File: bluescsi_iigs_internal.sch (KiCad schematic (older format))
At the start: 16 parts, among them J1 Conn_02x13_Top_Bottom, J2 Conn_02x13_Top_Bottom, J3 Micro_SD_Card, SW1 SW_SPDT, U1 YAAJ_BluePill, U2 UCC5606, U3 UCC5606

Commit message: V1.1 from v1.0 Fix IDC26 pin header to be correct! Change capacitor footprint to handsolder variant. Move mounting holes toward centre by about 2.54 and back by 2.54
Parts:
- C1, C2, C3: footprint Capacitor_Tantalum_SMD:CP_EIA-3528-21_Kemet-B -> Capacitor_Tantalum_SMD:CP_EIA-3528-21_Kemet-B_Pad1.50x2.35mm_HandSolder
- J1, J2: value Conn_02x13_Top_Bottom -> Conn_02x13_Odd_Even; symbol Connector_Generic:Conn_02x13_Top_Bottom -> Connector_Generic:Conn_02x13_Odd_Even
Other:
- moved on the sheet: D2, H1, H2, J3, R2, SW1

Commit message: Change switch to smd
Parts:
- SW1: footprint Connector_PinHeader_2.54mm:PinHeader_1x03_P2.54mm_Horizontal -> Button_Switch_SMD:SW_SPDT_PCM12
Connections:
- net +5V: now also SW1.3 (C); no longer SW1.1 (A)
- net GND: now also SW1.1 (A); no longer SW1.3 (C)
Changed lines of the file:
@@
 $EndComp
 $Comp
-L Switch:SW_SPDT SW1
-U 1 1 6062FC1A
-P 7300 1300
-F 0 "SW1" H 7300 1585 50  0000 C CNN
-F 1 "SW_SPDT" H 7300 1494 50  0000 C CNN
-F 2 "Connector_PinHeader_2.54mm:PinHeader_1x03_P2.54mm_Horizontal" H 7300 1300 50  0001 C CNN
-F 3 "~" H 7300 1300 50  0001 C CNN
-	1    7300 1300
-	1    0    0    -1
-$EndComp
-$Comp
 L Device:LED D2
 U 1 1 60631033
@@
 Text Label 1100 2050 2    50   ~ 0
 SCSI_DB6
+$Comp
+L Switch:SW_SPDT SW1
+U 1 1 6062FC1A
+P 7300 1300
+F 0 "SW1" H 7300 1585 50  0000 C CNN
+F 1 "SW_SPDT" H 7300 1494 50  0000 C CNN
+F 2 "Button_Switch_SMD:SW_SPDT_PCM12" H 7300 1300 50  0001 C CNN
+F 3 "~" H 7300 1300 50  0001 C CNN
+	1    7300 1300
+	1    0    0    1
+$EndComp
 $EndSCHEMATC

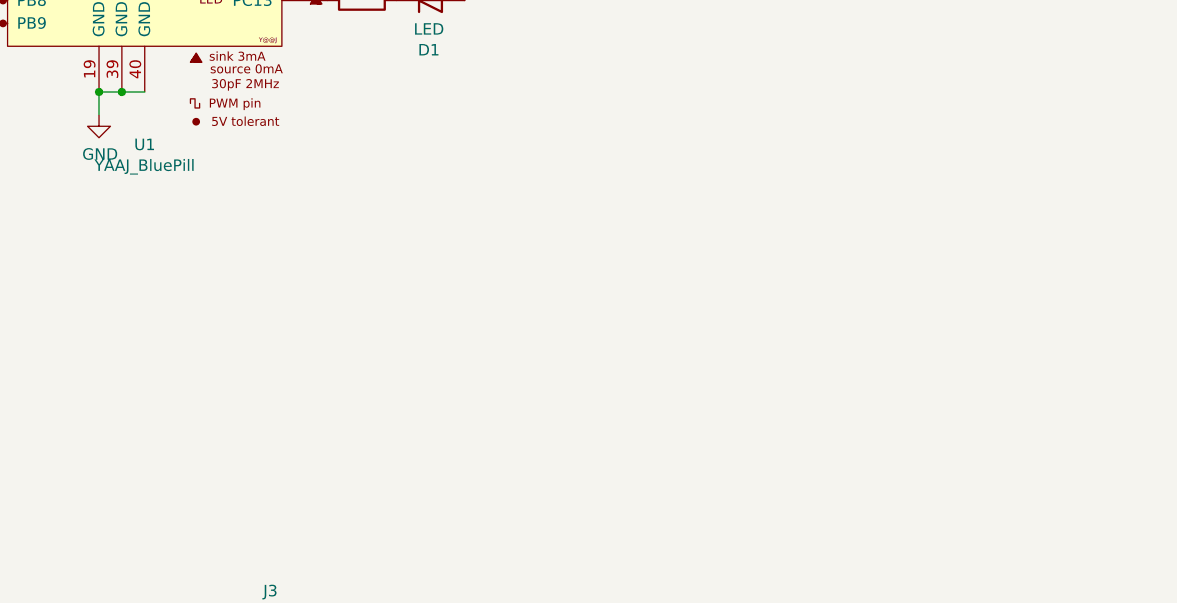
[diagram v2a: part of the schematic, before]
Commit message: Add auxilliary 12v input
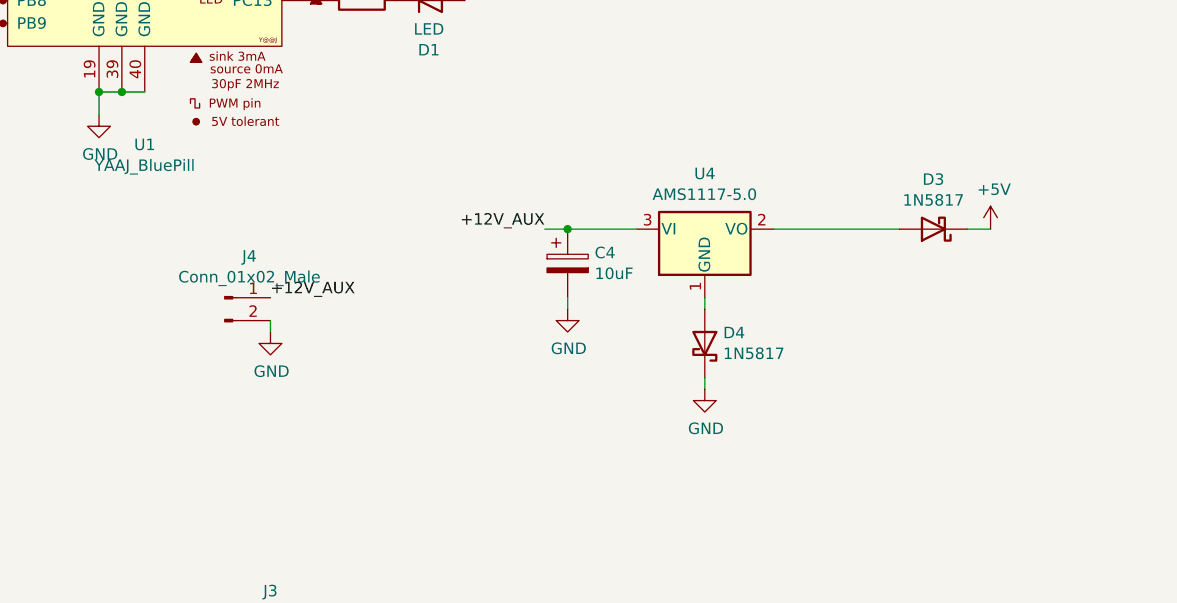
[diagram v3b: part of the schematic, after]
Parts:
- added C4: 10uF, Capacitor_Tantalum_SMD:CP_EIA-3528-21_Kemet-B_Pad1.50x2.35mm_HandSolder, symbol Device:CP
- added D3, D4: 1N5817, Diode_SMD:D_MicroMELF, symbol Device:D_Schottky
- added J4: Conn_01x02_Male, Connector_PinHeader_2.54mm:PinHeader_1x02_P2.54mm_Vertical, symbol Connector:Conn_01x02_Male
- added U4: AMS1117-5.0, Package_TO_SOT_SMD:SOT-223-3_TabPin2, symbol Regulator_Linear:AMS1117-5.0
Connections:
- net +5V: now also D3.1 (K)
- net GND: now also C4.2, D4.1 (K), J4.2 (Pin_2)
- new net: D4.2 (A), U4.1 (GND)
- new net: D3.2 (A), U4.2 (VO)
- new net +12V_AUX: C4.1, J4.1 (Pin_1), U4.3 (VI)
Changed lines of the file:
@@
 	1    0    0    1
 $EndComp
+$Comp
+L Regulator_Linear:AMS1117-5.0 U4
+U 1 1 608623C0
+P 7750 4550
+F 0 "U4" H 7750 4792 50  0000 C CNN
+F 1 "AMS1117-5.0" H 7750 4701 50  0000 C CNN
+F 2 "Package_TO_SOT_SMD:SOT-223-3_TabPin2" H 7750 4750 50  0001 C CNN
+F 3 "http://www.advanced-monolithic.com/pdf/ds1117.pdf" H 7850 4300 50  0001 C CNN
+	1    7750 4550
+	1    0    0    -1
+$EndComp
+$Comp
+L Device:CP C4
+U 1 1 608634DB
+P 7150 4700
+F 0 "C4" H 7268 4746 50  0000 L CNN
+F 1 "10uF" H 7268 4655 50  0000 L CNN
+F 2 "Capacitor_Tantalum_SMD:CP_EIA-3528-21_Kemet-B_Pad1.50x2.35mm_HandSolder" H 7188 4550 50  0001 C CNN
+F 3 "~" H 7150 4700 50  0001 C CNN
+	1    7150 4700
+	1    0    0    -1
+$EndComp
+$Comp
+L Connector:Conn_01x02_Male J4
+U 1 1 60864BE9
+P 5650 4850
+F 0 "J4" H 5758 5031 50  0000 C CNN
+F 1 "Conn_01x02_Male" H 5758 4940 50  0000 C CNN
+F 2 "Connector_PinHeader_2.54mm:PinHeader_1x02_P2.54mm_Vertical" H 5650 4850 50  0001 C CNN
+F 3 "~" H 5650 4850 50  0001 C CNN
+	1    5650 4850
+	1    0    0    -1
+$EndComp
+$Comp
+L power:GND #PWR0119
+U 1 1 60865DDA
+P 5850 5000
+F 0 "#PWR0119" H 5850 4750 50  0001 C CNN
+F 1 "GND" H 5855 4827 50  0000 C CNN
+F 2 "" H 5850 5000 50  0001 C CNN
+F 3 "" H 5850 5000 50  0001 C CNN
+	1    5850 5000
+	1    0    0    -1
+$EndComp
+$Comp
+L power:GND #PWR0120
+U 1 1 6086659F
+P 7150 4900
+F 0 "#PWR0120" H 7150 4650 50  0001 C CNN
+F 1 "GND" H 7155 4727 50  0000 C CNN
+F 2 "" H 7150 4900 50  0001 C CNN
+F 3 "" H 7150 4900 50  0001 C CNN
+	1    7150 4900
+	1    0    0    -1
+$EndComp
+$Comp
+L power:GND #PWR0121
+U 1 1 60866B00
+P 7750 5250
+F 0 "#PWR0121" H 7750 5000 50  0001 C CNN
+F 1 "GND" H 7755 5077 50  0000 C CNN
+F 2 "" H 7750 5250 50  0001 C CNN
+F 3 "" H 7750 5250 50  0001 C CNN
+	1    7750 5250
+	1    0    0    -1
+$EndComp
+Wire Wire Line
+	5850 4950 5850 5000
+Text Label 5850 4850 0    50   ~ 0
++12V_AUX
+Text Label 7050 4550 2    50   ~ 0
++12V_AUX
+Wire Wire Line
+	7050 4550 7150 4550
+Wire Wire Line
+	7150 4550 7450 4550
+Connection ~ 7150 4550
+Wire Wire Line
+	7150 4850 7150 4900
+Wire Wire Line
+	7750 4850 7750 4900
+$Comp
+L Device:D_Schottky D3
+U 1 1 6086E55B
+P 8750 4550
+F 0 "D3" H 8750 4333 50  0000 C CNN
+F 1 "1N5817" H 8750 4424 50  0000 C CNN
+F 2 "Diode_SMD:D_MicroMELF" H 8750 4550 50  0001 C CNN
+F 3 "~" H 8750 4550 50  0001 C CNN
+	1    8750 4550
+	-1   0    0    1
+$EndComp
+$Comp
+L Device:D_Schottky D4
+U 1 1 6086EF1B
+P 7750 5050
+F 0 "D4" V 7796 5130 50  0000 L CNN
+F 1 "1N5817" V 7705 5130 50  0000 L CNN
+F 2 "Diode_SMD:D_MicroMELF" H 7750 5050 50  0001 C CNN
+F 3 "~" H 7750 5050 50  0001 C CNN
+	1    7750 5050
+	0    1    -1   0
+$EndComp
+Wire Wire Line
+	7750 5200 7750 5250
+$Comp
+L power:+5V #PWR0123
+U 1 1 6087347C
+P 9000 4550
+F 0 "#PWR0123" H 9000 4400 50  0001 C CNN
+F 1 "+5V" H 9015 4723 50  0000 C CNN
+F 2 "" H 9000 4550 50  0001 C CNN
+F 3 "" H 9000 4550 50  0001 C CNN
+	1    9000 4550
+	1    0    0    -1
+$EndComp
+Wire Wire Line
+	8900 4550 9000 4550
+Wire Wire Line
+	8050 4550 8600 4550
 $EndSCHEMATC

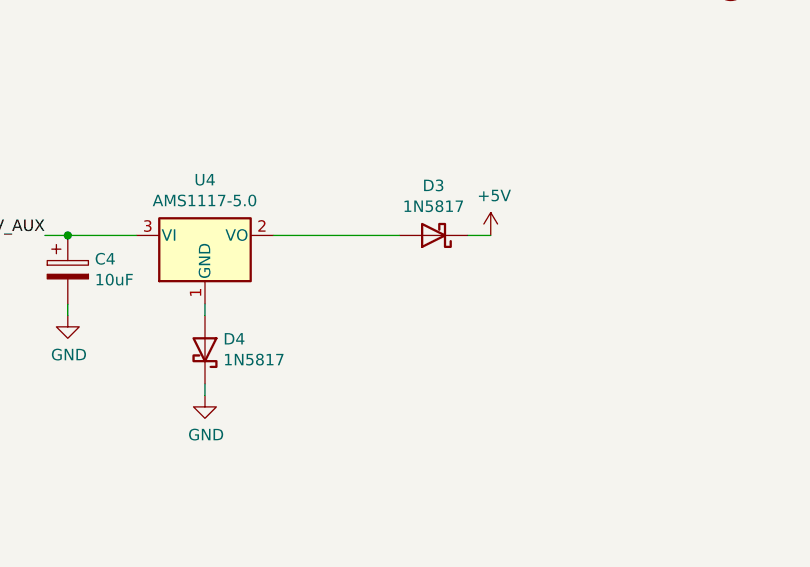
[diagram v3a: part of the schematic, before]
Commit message: Change footprint of diodes
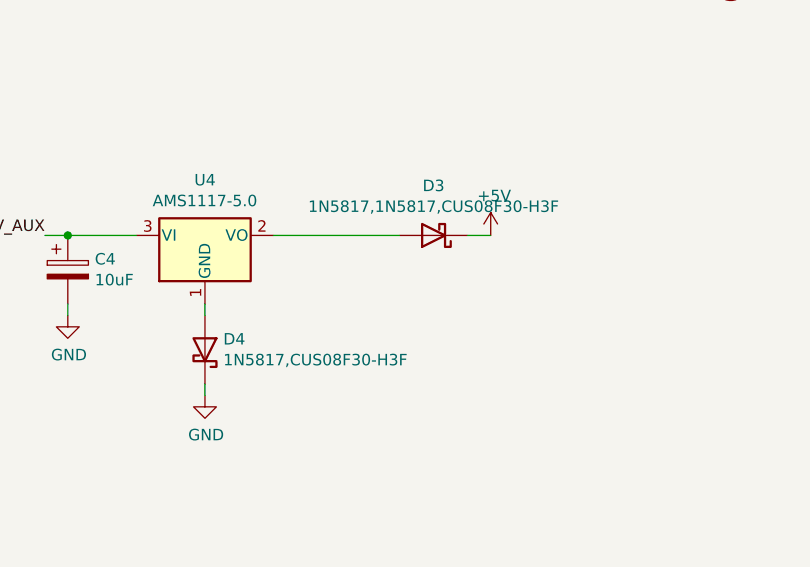
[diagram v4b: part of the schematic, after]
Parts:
- D3: value 1N5817 -> 1N5817,1N5817,CUS08F30-H3F; footprint Diode_SMD:D_MicroMELF -> Diode_SMD:D_SOD-323_HandSoldering
- D4: value 1N5817 -> 1N5817,CUS08F30-H3F; footprint Diode_SMD:D_MicroMELF -> Diode_SMD:D_SOD-323_HandSoldering
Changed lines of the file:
@@
 P 8750 4550
 F 0 "D3" H 8750 4333 50  0000 C CNN
-F 1 "1N5817" H 8750 4424 50  0000 C CNN
-F 2 "Diode_SMD:D_MicroMELF" H 8750 4550 50  0001 C CNN
+F 1 "1N5817,1N5817,CUS08F30-H3F" H 8750 4424 50  0000 C CNN
+F 2 "Diode_SMD:D_SOD-323_HandSoldering" H 8750 4550 50  0001 C CNN
 F 3 "~" H 8750 4550 50  0001 C CNN
 	1    8750 4550
@@
 P 7750 5050
 F 0 "D4" V 7796 5130 50  0000 L CNN
-F 1 "1N5817" V 7705 5130 50  0000 L CNN
-F 2 "Diode_SMD:D_MicroMELF" H 7750 5050 50  0001 C CNN
+F 1 "1N5817,CUS08F30-H3F" V 7705 5130 50  0000 L CNN
+F 2 "Diode_SMD:D_SOD-323_HandSoldering" H 7750 5050 50  0001 C CNN
 F 3 "~" H 7750 5050 50  0001 C CNN
 	1    7750 5050

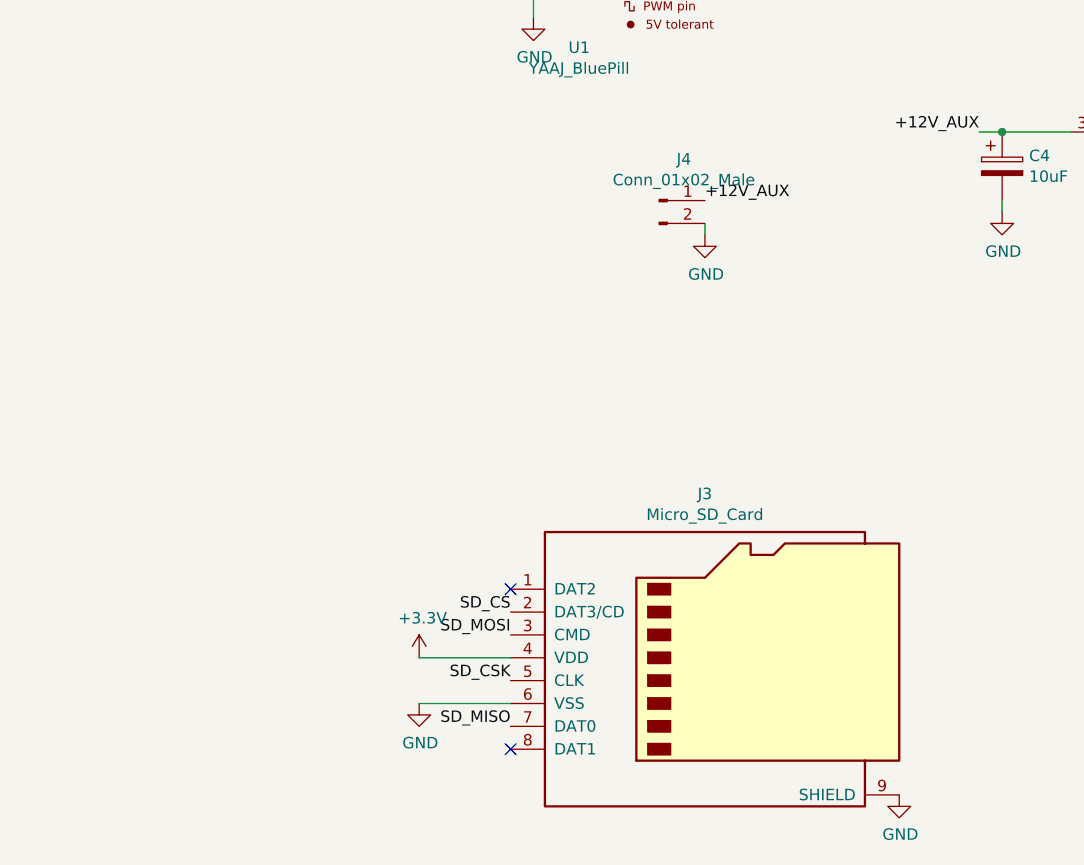
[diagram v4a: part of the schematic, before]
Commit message: Change microsd slot to Molex 105162-0001. Add version number to back silkscreen
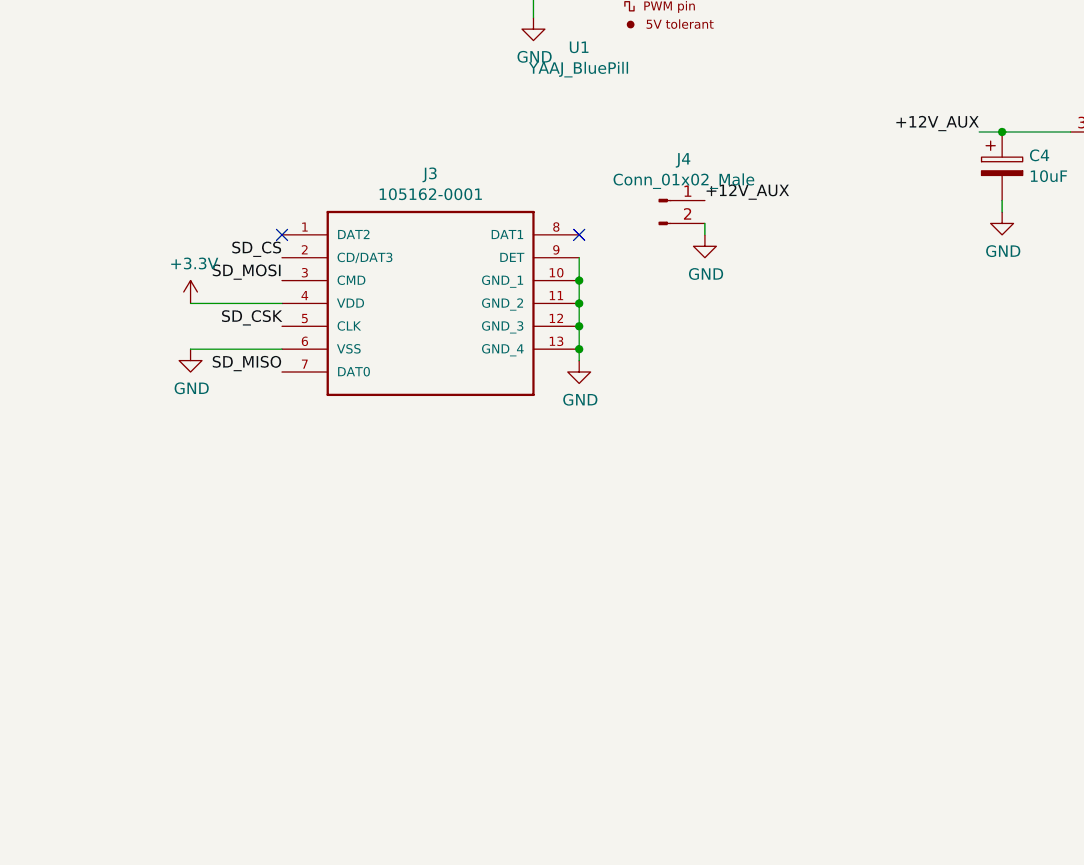
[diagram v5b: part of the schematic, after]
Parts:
- removed J3: Micro_SD_Card, Connector_Card:microSD_HC_Molex_104031-0811, symbol Connector:Micro_SD_Card
- added J3: 105162-0001, 105162-0001, symbol 105162-0001:105162-0001
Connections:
- net +3V3: now also J3.4 (VDD)
- net GND: now also J3.10 (GND_1), J3.11 (GND_2), J3.12 (GND_3), J3.13 (GND_4), J3.6 (VSS), J3.9 (DET)
- net SD_CS: now also J3.2 (CD/DAT3)
- net SD_CSK: now also J3.5 (CLK)
- net SD_MISO: now also J3.7 (DAT0)
- net SD_MOSI: now also J3.3 (CMD)
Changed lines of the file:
@@
 L power:+3.3V #PWR0105
 U 1 1 6061CFE5
-P 4600 6850
-F 0 "#PWR0105" H 4600 6700 50  0001 C CNN
-F 1 "+3.3V" H 4615 7023 50  0000 C CNN
-F 2 "" H 4600 6850 50  0001 C CNN
-F 3 "" H 4600 6850 50  0001 C CNN
-	1    4600 6850
+P 3600 5300
+F 0 "#PWR0105" H 3600 5150 50  0001 C CNN
+F 1 "+3.3V" H 3615 5473 50  0000 C CNN
+F 2 "" H 3600 5300 50  0001 C CNN
+F 3 "" H 3600 5300 50  0001 C CNN
+	1    3600 5300
 	1    0    0    -1
 $EndComp
@@
 SD_MOSI
 $Comp
-L Connector:Micro_SD_Card J3
-U 1 1 6062225F
-P 5900 6850
-F 0 "J3" H 5850 7567 50  0000 C CNN
-F 1 "Micro_SD_Card" H 5850 7476 50  0000 C CNN
-F 2 "Connector_Card:microSD_HC_Molex_104031-0811" H 7050 7150 50  0001 C CNN
-F 3 "http://katalog.we-online.de/em/datasheet/693072010801.pdf" H 5900 6850 50  0001 C CNN
-	1    5900 6850
-	1    0    0    -1
-$EndComp
-$Comp
 L power:GND #PWR0108
 U 1 1 60623212
-P 4600 7050
-F 0 "#PWR0108" H 4600 6800 50  0001 C CNN
-F 1 "GND" H 4605 6877 50  0000 C CNN
-F 2 "" H 4600 7050 50  0001 C CNN
-F 3 "" H 4600 7050 50  0001 C CNN
-	1    4600 7050
+P 5300 5550
+F 0 "#PWR0108" H 5300 5300 50  0001 C CNN
+F 1 "GND" H 5305 5377 50  0000 C CNN
+F 2 "" H 5300 5550 50  0001 C CNN
+F 3 "" H 5300 5550 50  0001 C CNN
+	1    5300 5550
 	1    0    0    -1
 $EndComp
-Text Label 5000 6650 2    50   ~ 0
+Text Label 4000 5100 2    50   ~ 0
 SD_CS
-Text Label 5000 6950 2    50   ~ 0
+Text Label 4000 5400 2    50   ~ 0
 SD_CSK
-Text Label 5000 7150 2    50   ~ 0
+Text Label 4000 5600 2    50   ~ 0
 SD_MISO
-Text Label 5000 6750 2    50   ~ 0
+Text Label 4000 5200 2    50   ~ 0
 SD_MOSI
-$Comp
-L power:GND #PWR0109
-U 1 1 60623E38
-P 6700 7450
-F 0 "#PWR0109" H 6700 7200 50  0001 C CNN
-F 1 "GND" H 6705 7277 50  0000 C CNN
-F 2 "" H 6700 7450 50  0001 C CNN
-F 3 "" H 6700 7450 50  0001 C CNN
-	1    6700 7450
-	1    0    0    -1
-$EndComp
-Wire Wire Line
-	4600 6850 5000 6850
 Wire Wire Line
-	5000 7050 4600 7050
-NoConn ~ 5000 7250
-NoConn ~ 5000 6550
+	3600 5300 4000 5300
+NoConn ~ 5300 5000
+NoConn ~ 4000 5000
 $Comp
 L Mechanical:MountingHole H1
@@
 Wire Wire Line
 	8050 4550 8600 4550
+$Comp
+L 105162-0001:105162-0001 J3
+U 1 1 6089B89F
+P 4000 5000
+F 0 "J3" H 4650 5267 50  0000 C CNN
+F 1 "105162-0001" H 4650 5176 50  0000 C CNN
+F 2 "105162-0001" H 4000 5000 50  0001 L BNN
+F 3 "" H 4000 5000 50  0001 L BNN
+F 4 "Memory Card Connectors 1.45H MICRO SD HEADER WITH D/C PIN" H 4000 5000 50  0001 L BNN "DESCRIPTION"
+F 5 "mm" H 4000 5000 50  0001 L BNN "HEIGHT"
+F 6 "https://www.mouser.co.uk/ProductDetail/Molex/105162-0001?qs=1fNsfHe5VsK8daqlgKxZfQ%3D%3D" H 4000 5000 50  0001 L BNN "MOUSER_PRICE-STOCK"
+F 7 "538-105162-0001" H 4000 5000 50  0001 L BNN "MOUSER_PART_NUMBER"
+F 8 "Molex" H 4000 5000 50  0001 L BNN "MANUFACTURER_NAME"
+F 9 "105162-0001" H 4000 5000 50  0001 L BNN "MANUFACTURER_PART_NUMBER"
+	1    4000 5000
+	1    0    0    -1
+$EndComp
+Wire Wire Line
+	5300 5100 5300 5200
+Connection ~ 5300 5200
+Wire Wire Line
+	5300 5200 5300 5300
+Connection ~ 5300 5300
+Wire Wire Line
+	5300 5300 5300 5400
+Connection ~ 5300 5400
+Wire Wire Line
+	5300 5400 5300 5500
+Connection ~ 5300 5500
+Wire Wire Line
+	5300 5500 5300 5550
+$Comp
+L power:GND #PWR0109
+U 1 1 6089E2A4
+P 3600 5500
+F 0 "#PWR0109" H 3600 5250 50  0001 C CNN
+F 1 "GND" H 3605 5327 50  0000 C CNN
+F 2 "" H 3600 5500 50  0001 C CNN
+F 3 "" H 3600 5500 50  0001 C CNN
+	1    3600 5500
+	1    0    0    -1
+$EndComp
+Wire Wire Line
+	4000 5500 3600 5500
 $EndSCHEMATC
